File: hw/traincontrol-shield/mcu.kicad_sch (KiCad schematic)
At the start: 7 parts, among them J1 ESP32-S3 Header L, J2 ESP32-S3 Header R

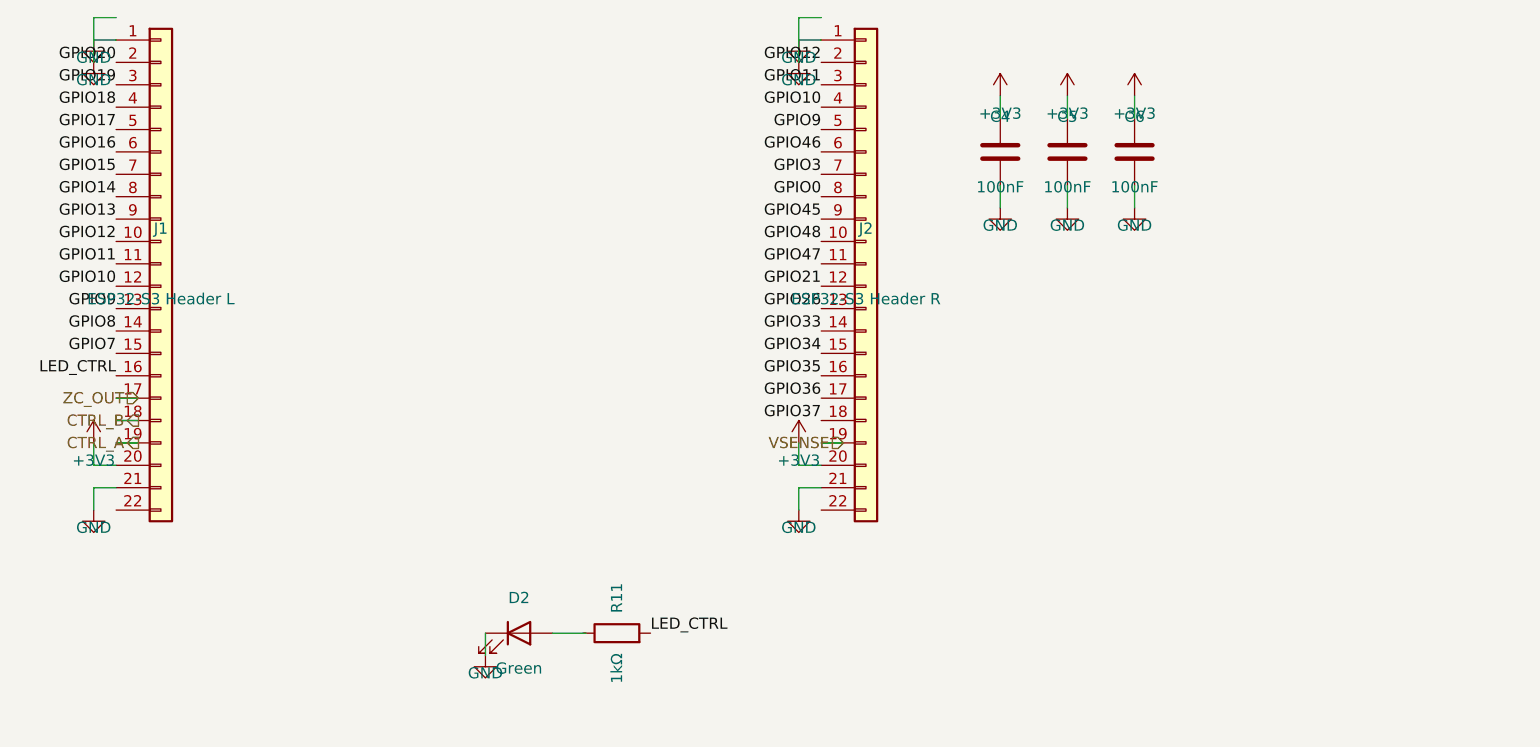
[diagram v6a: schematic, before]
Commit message: Disperse component layout and triple wire stub length across all sheets
- STUB: 2.54 → 7.62 mm (3×) in all three generator scripts
- Inter-component spacing doubled in power-supply, MCU, and logic sheets
- Top-level inter-column gap widened (LX 120 → 130 mm) to avoid label collision
- Sheet frame heights made variable per pin count (20–35 mm)
- Right-column sheet x-origin and connector J4/J5/J6 x-positions updated accordingly
- All 8 sheets regenerated and validated with kicad-cli

Co-Authored-By: Claude Sonnet 4.6 <noreply@anthropic.com>
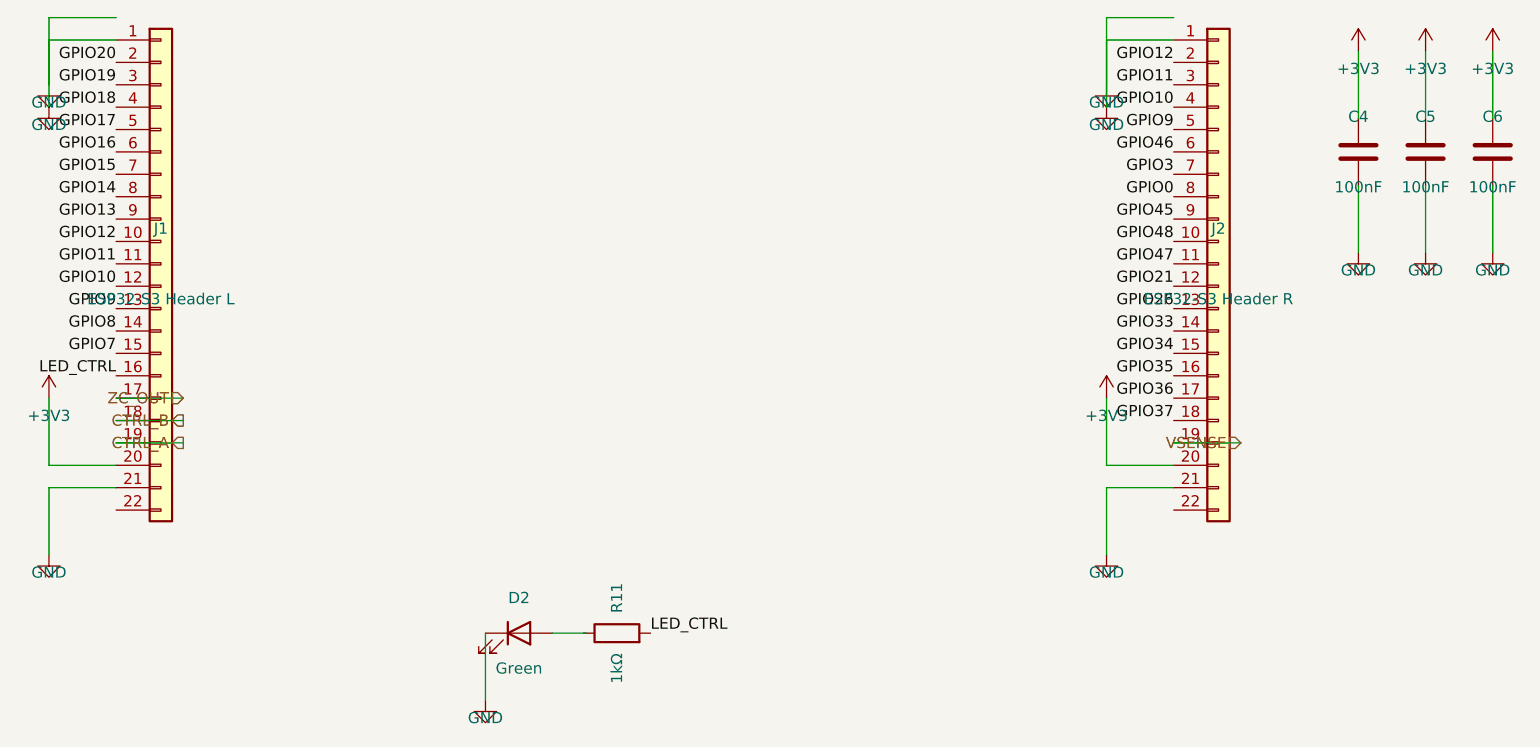
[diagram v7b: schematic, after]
